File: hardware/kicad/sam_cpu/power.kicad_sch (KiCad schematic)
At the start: 35 parts, among them J11 J11 POWER, J17 EXT 5V, J23 EXT 12V, U1 TPS2117, U3 NCP1117-3.3

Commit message: Clean +12 V rail (ideal-diode OR of J23 and J11 pin 6) and a Pi buck with BUCK / BOARD jumpers
c42 (schematic): LTC4412 + DMP3013SFV per input into F1, external priority via
the U34 CTL divider; TPS54302 buck to PI_5V_BUCK; JP4 BUCK / JP3 BOARD pick the
J21 5 V (both open for a Jetson). c43 (board): OR by J23, buck under the Pi,
JP3 cuts the +5V trunk to J21, all hand-routed; 23 unconnected as before, no
new DRC errors.

Co-Authored-By: Claude Opus 5.5 <noreply@anthropic.com>
Claude-Session: https://claude.ai/code/session_01QQate2kninVTv93dgZ4pfZ
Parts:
- added C133, C134: 10u, Capacitor_SMD:C_1206_3216Metric, symbol Device:C
- added C135, C136: 22u, Capacitor_SMD:C_1206_3216Metric, symbol Device:C
- added C137: 100n, Capacitor_SMD:C_0603_1608Metric, symbol Device:C
- added JP3: BOARD, Jumper:SolderJumper-2_P1.3mm_Open_RoundedPad1.0x1.5mm, symbol Jumper:SolderJumper_2_Open
- added JP4: BUCK, Jumper:SolderJumper-2_P1.3mm_Open_RoundedPad1.0x1.5mm, symbol Jumper:SolderJumper_2_Open
- added L2: 10u, Inductor_SMD:L_Changjiang_FXL0630, symbol Device:L
- added Q19, Q20: DMP3013SFV, Package_SON:Diodes_PowerDI3333-8, symbol Transistor_FET:DMP3013SFV
- added R213: 47k, Resistor_SMD:R_0603_1608Metric, symbol Device:R
- added R214: 10k, Resistor_SMD:R_0603_1608Metric, symbol Device:R
- added R215: 100k, Resistor_SMD:R_0603_1608Metric, symbol Device:R
- added R216: 13k, Resistor_SMD:R_0603_1608Metric, symbol Device:R
- added U33, U34: LTC4412, Package_TO_SOT_SMD:TSOT-23-6, symbol Power_Management:LTC4412xS6
- added U35: TPS54302, Package_TO_SOT_SMD:SOT-23-6, symbol Regulator_Switching:TPS54302
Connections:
- net +12V: now also C133.1, C134.1, U35.3 (VIN)
- net +5V: now also JP3.1 (A)
- net GND: now also C133.2, C134.2, C135.2, C136.2, R214.2, R216.2, U33.2 (GND), U33.3 (CTL), U34.2 (GND), U35.1 (GND)
- net 12V_OR: now reaches F1.1
- net 12V_OR: now also Q19.1 (S), Q19.2 (S), Q19.3 (S), Q20.1 (S), Q20.2 (S), Q20.3 (S), U33.6 (SENSE), U34.6 (SENSE); no longer J23.1 (Pin_1)
- net IO_12V: now reaches J11.6 (Pin_6)
- net IO_12V: now also Q20.5 (D), U34.1 (VIN)
- new net: C137.2, L2.1, U35.2 (SW)
- new net: R215.2, R216.1, U35.4 (FB)
- new net: C137.1, U35.6 (BOOT)
- new net: R213.2, R214.1, U34.3 (CTL)
- new net: Q19.4 (G), U33.5 (GATE)
- new net: Q20.4 (G), U34.5 (GATE)
- new net EXT_12V: J23.1 (Pin_1), Q19.5 (D), R213.1, U33.1 (VIN)
- new net PI_5V: JP3.2 (B), JP4.1 (A)
- new net PI_5V_BUCK: C135.1, C136.1, JP4.2 (B), L2.2, R215.1
- no-connect marks 3 -> 5
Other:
- note added: "+12 V OR (12V_OR to F1): J23 external (priority) or J11 pin 6 (IO board)"
- note added: "External +12 V (J23) and rail fuse F1"
- note added: "IO board power (J11: +5 V, +12 V on pin 6)"
- note added: "J11 keeps the original CPU board connector (IO board J16 harness): +5 V, ground and +12 V (pin 6, unregulated); -12 V (pin 3) is not used. The +12 V rail (audio amplifiers, Pi buck) comes from J23 (external, priority) or J11 pin 6 through ideal diodes U33 / U34 (they block reverse polarity), then F1 (4 A hold) and the D5 clamp. U3 NCP1117 (as in the RP2350 hardware guide) is stable with ceramic c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"
- note added: "JP3 / JP4 (open by default) feed J21 pins 2 / 4 (PI_5V): JP4: from the buck (Pi 4 / Pi 5, 5.18 V 3 A) JP3: from the board +5 V both open: Jetson, or a Pi on its own USB-C. Never bridge both."
- note added: "Pi 5.1 V buck (3 A) and Pi header 5 V jumpers JP3 / JP4"
- note removed: "External +12 V for audio (J23)"
- note removed: "IO board power (J11, +5 V only)"
- note removed: "J11 keeps the original CPU board connector (IO board J16 harness) for +5 V and ground only: its +-12 V pins are not used. The audio amplifiers run from an external +12 V supply on J23 (about 3 A at full volume). F1 + D5 blow the fuse on reverse polarity. U3 NCP1117 (as in the RP2350 hardware guide) is stable with ceramic capacitors. All regulator capacitors are 0805 or larger for low DC-bias dera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"
- title: Power: +5 V mux, external +12 V, 3.3 V, 4.5 V, monitors -> Power: +5 V mux, +12 V OR, Pi buck, 3.3 V, 4.5 V, monitors

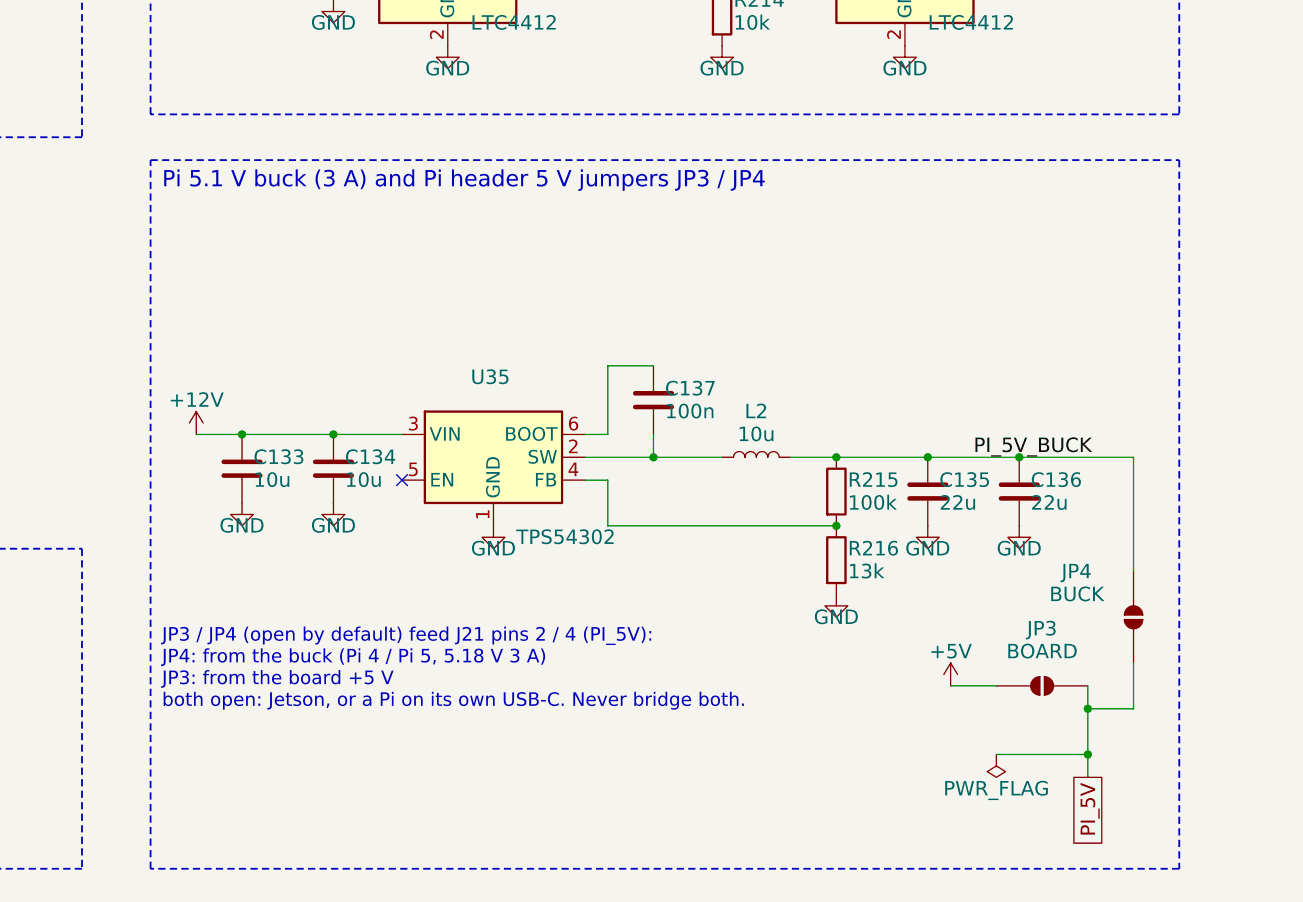
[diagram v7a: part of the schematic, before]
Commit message: Pi header 5 V: one three-pad solder jumper JP3 instead of JP3 + JP4
Two separate jumpers could both be bridged. c44 (schematic) and c45 (board)
put one SolderJumper_3 by the buck: 1-2 buck, 2-3 board +5 V, open for a
Jetson. The +5V trunk is whole again inside the DeepPCB cut and is cut on
x 109 by the buck instead; 23 unconnected as before, no new DRC errors.

Co-Authored-By: Claude Opus 5.5 <noreply@anthropic.com>
Claude-Session: https://claude.ai/code/session_01QQate2kninVTv93dgZ4pfZ
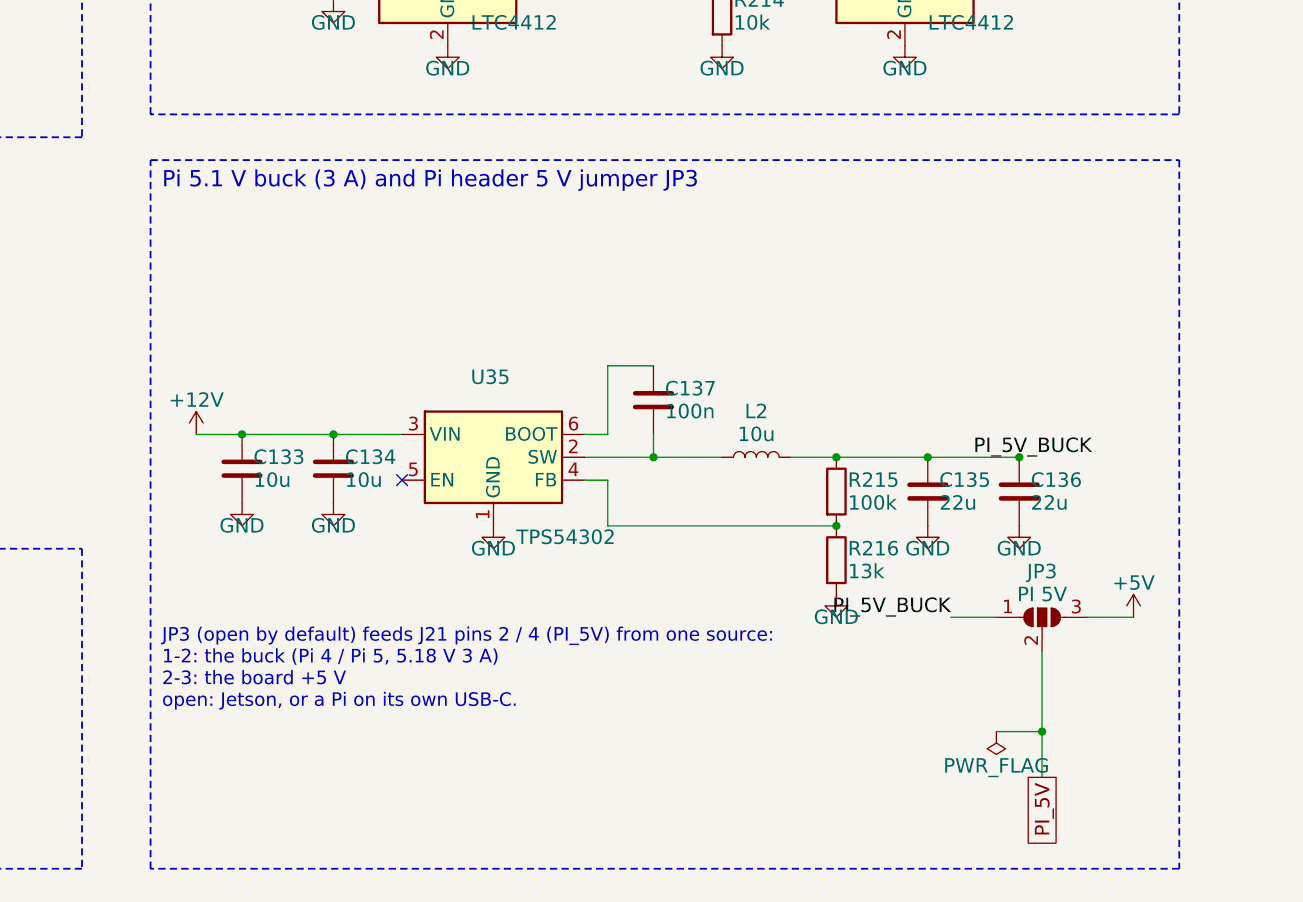
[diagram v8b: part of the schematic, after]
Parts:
- removed JP3: BOARD, Jumper:SolderJumper-2_P1.3mm_Open_RoundedPad1.0x1.5mm, symbol Jumper:SolderJumper_2_Open
- removed JP4: BUCK, Jumper:SolderJumper-2_P1.3mm_Open_RoundedPad1.0x1.5mm, symbol Jumper:SolderJumper_2_Open
- added JP3: PI 5V, Jumper:SolderJumper-3_P1.3mm_Open_RoundedPad1.0x1.5mm, symbol Jumper:SolderJumper_3_Open
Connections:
- net +5V: now also JP3.3 (B)
- net PI_5V: now also JP3.2 (C)
- net PI_5V_BUCK: now also JP3.1 (A)
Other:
- note added: "JP3 (open by default) feeds J21 pins 2 / 4 (PI_5V) from one source: 1-2: the buck (Pi 4 / Pi 5, 5.18 V 3 A) 2-3: the board +5 V open: Jetson, or a Pi on its own USB-C."
- note added: "Pi 5.1 V buck (3 A) and Pi header 5 V jumper JP3"
- note removed: "JP3 / JP4 (open by default) feed J21 pins 2 / 4 (PI_5V): JP4: from the buck (Pi 4 / Pi 5, 5.18 V 3 A) JP3: from the board +5 V both open: Jetson, or a Pi on its own USB-C. Never bridge both."
- note removed: "Pi 5.1 V buck (3 A) and Pi header 5 V jumpers JP3 / JP4"
